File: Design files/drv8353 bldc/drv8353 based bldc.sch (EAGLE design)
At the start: 115 parts, among them IC1 DRV8353RSRGZT, J3 2X6 FEMALE, J4 B06B-HCMKK

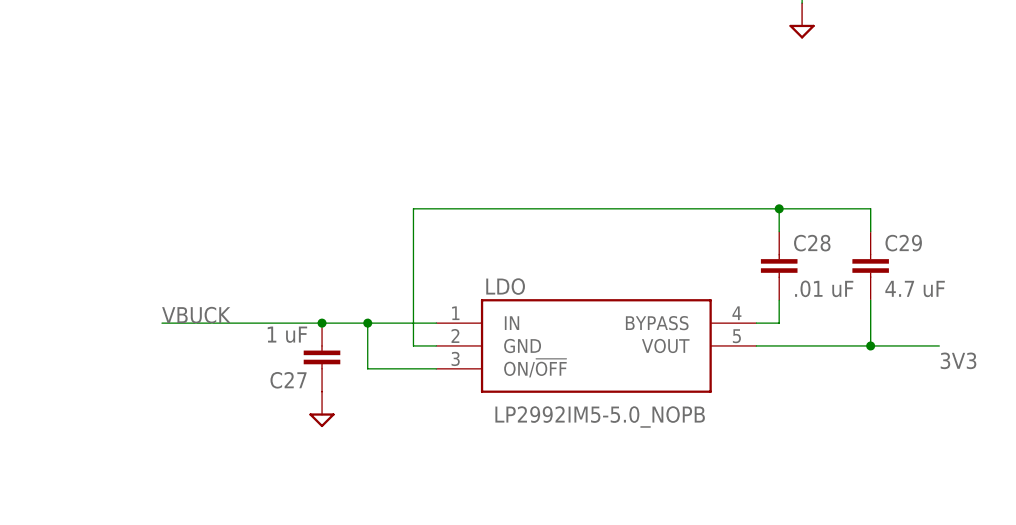
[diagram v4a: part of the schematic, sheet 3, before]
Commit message: adds zener and bypas header for LDO
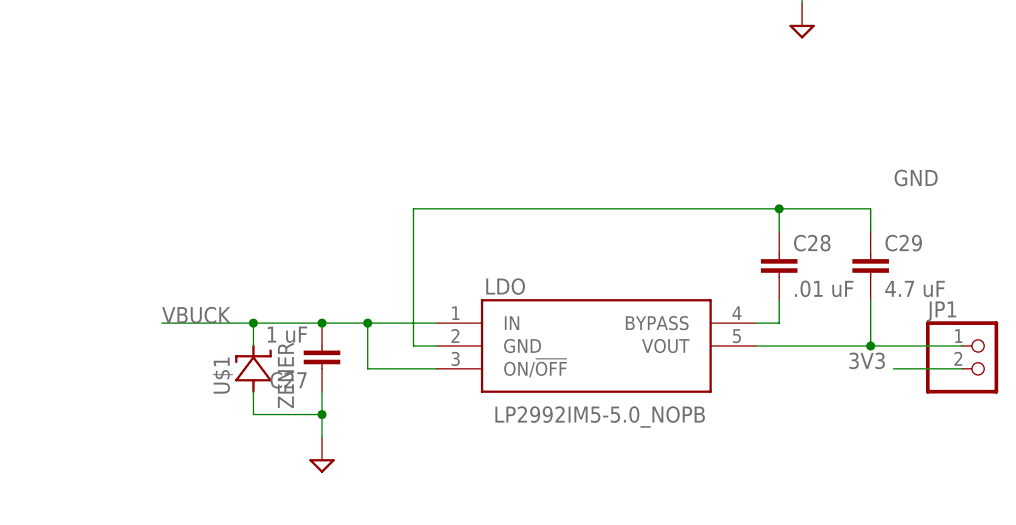
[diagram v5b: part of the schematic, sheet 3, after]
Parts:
- added JP1: (no value), pinhead:PINHD-1X2
- added U$1: ZENER, REV BLDC:ZENER
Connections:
- removed net N$5: C28.1, C29.1, LDO.GND
- new net N$2: C29.2, JP1.1, LDO.VOUT
- net 3V3: now also JP1.2; no longer C29.2, LDO.VOUT
- net GND: now also C28.1, C29.1, LDO.GND, U$1.A
- net VBUCK: now also U$1.C
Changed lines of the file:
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@@
 <part name="D6" library="REV BLDC" deviceset="D-" device="SOD123" package3d_urn="urn:adsk.eagle:package:26308/2"/>
 <part name="D7" library="REV BLDC" deviceset="D-" device="SOD123" package3d_urn="urn:adsk.eagle:package:26308/2"/>
+<part name="U$1" library="REV BLDC" deviceset="ZENER" device="" package3d_urn="urn:adsk.eagle:package:26308/2"/>
+<part name="JP1" library="pinhead" library_urn="urn:adsk.eagle:library:325" deviceset="PINHD-1X2" device="" package3d_urn="urn:adsk.eagle:package:22435/2"/>
 </parts>
 <sheets>
@@
 <attribute name="VALUE" x="197.104" y="0.381" size="1.778" layer="96"/>
 </instance>
-<instance part="SUPPLY7" gate="GND" x="134.62" y="-12.7" smashed="yes"/>
+<instance part="SUPPLY7" gate="GND" x="134.62" y="-17.78" smashed="yes"/>
 <instance part="J4" gate="G$1" x="25.4" y="-15.24" smashed="yes">
 <attribute name="NAME" x="41.91" y="-7.62" size="1.778" layer="95" align="center-left"/>
@@
 <instance part="U$7" gate="G$1" x="55.88" y="10.16" smashed="yes"/>
 <instance part="U$8" gate="G$1" x="55.88" y="7.62" smashed="yes"/>
+<instance part="U$1" gate="G$1" x="127" y="-7.62" smashed="yes" rot="R90">
+<attribute name="NAME" x="124.3584" y="-10.5664" size="1.778" layer="95" rot="R90"/>
+<attribute name="VALUE" x="131.4958" y="-12.0904" size="1.778" layer="96" rot="R90"/>
+</instance>
+<instance part="JP1" gate="G$1" x="208.28" y="-7.62" smashed="yes">
+<attribute name="NAME" x="201.93" y="-1.905" size="1.778" layer="95"/>
+<attribute name="VALUE" x="201.93" y="-12.7" size="1.778" layer="96"/>
+</instance>
 </instances>
 <busses>
@@
 <pinref part="C27" gate="G$1" pin="1"/>
 <pinref part="SUPPLY7" gate="GND" pin="GND"/>
+<wire x1="134.62" y1="-15.24" x2="134.62" y2="-12.7" width="0.1524" layer="91"/>
+<pinref part="U$1" gate="G$1" pin="A"/>
+<wire x1="134.62" y1="-12.7" x2="134.62" y2="-10.16" width="0.1524" layer="91"/>
+<wire x1="127" y1="-10.16" x2="127" y2="-12.7" width="0.1524" layer="91"/>
+<wire x1="127" y1="-12.7" x2="134.62" y2="-12.7" width="0.1524" layer="91"/>
+<junction x="134.62" y="-12.7"/>
 </segment>
 <segment>
@@
 <wire x1="45.72" y1="-20.32" x2="55.88" y2="-20.32" width="0.1524" layer="91"/>
 <label x="55.88" y="-20.32" size="1.778" layer="95"/>
+</segment>
+<segment>
+<pinref part="LDO" gate="G$1" pin="GND"/>
+<wire x1="147.32" y1="-5.08" x2="144.78" y2="-5.08" width="0.1524" layer="91"/>
+<wire x1="144.78" y1="-5.08" x2="144.78" y2="10.16" width="0.1524" layer="91"/>
+<wire x1="144.78" y1="10.16" x2="185.42" y2="10.16" width="0.1524" layer="91"/>
+<pinref part="C28" gate="G$1" pin="1"/>
+<wire x1="185.42" y1="10.16" x2="195.58" y2="10.16" width="0.1524" layer="91"/>
+<wire x1="185.42" y1="7.62" x2="185.42" y2="10.16" width="0.1524" layer="91"/>
+<junction x="185.42" y="10.16"/>
+<pinref part="C29" gate="G$1" pin="1"/>
+<wire x1="195.58" y1="7.62" x2="195.58" y2="10.16" width="0.1524" layer="91"/>
+<label x="198.12" y="12.7" size="1.778" layer="95"/>
 </segment>
 </net>
@@
 <pinref part="LDO" gate="G$1" pin="ON/!OFF"/>
 <wire x1="139.7" y1="-2.54" x2="134.62" y2="-2.54" width="0.1524" layer="91"/>
-<wire x1="134.62" y1="-2.54" x2="116.84" y2="-2.54" width="0.1524" layer="91"/>
+<wire x1="134.62" y1="-2.54" x2="127" y2="-2.54" width="0.1524" layer="91"/>
+<wire x1="127" y1="-2.54" x2="116.84" y2="-2.54" width="0.1524" layer="91"/>
 <wire x1="147.32" y1="-7.62" x2="139.7" y2="-7.62" width="0.1524" layer="91"/>
 <wire x1="139.7" y1="-7.62" x2="139.7" y2="-2.54" width="0.1524" layer="91"/>
@@
 <pinref part="C27" gate="G$1" pin="2"/>
 <junction x="134.62" y="-2.54"/>
+<pinref part="U$1" gate="G$1" pin="C"/>
+<wire x1="127" y1="-5.08" x2="127" y2="-2.54" width="0.1524" layer="91"/>
+<junction x="127" y="-2.54"/>
 </segment>
 </net>
 <net name="3V3" class="0">
-<segment>
-<pinref part="LDO" gate="G$1" pin="VOUT"/>
-<wire x1="182.88" y1="-5.08" x2="195.58" y2="-5.08" width="0.1524" layer="91"/>
-<pinref part="C29" gate="G$1" pin="2"/>
-<wire x1="195.58" y1="-5.08" x2="203.2" y2="-5.08" width="0.1524" layer="91"/>
-<wire x1="195.58" y1="0" x2="195.58" y2="-5.08" width="0.1524" layer="91"/>
-<junction x="195.58" y="-5.08"/>
-<label x="203.2" y="-7.62" size="1.778" layer="95"/>
-</segment>
 <segment>
 <pinref part="J4" gate="G$1" pin="2"/>
@@
 <label x="55.88" y="-15.24" size="1.778" layer="95"/>
 </segment>
-</net>
-<net name="N$5" class="0">
-<segment>
-<pinref part="LDO" gate="G$1" pin="GND"/>
-<wire x1="147.32" y1="-5.08" x2="144.78" y2="-5.08" width="0.1524" layer="91"/>
-<wire x1="144.78" y1="-5.08" x2="144.78" y2="10.16" width="0.1524" layer="91"/>
-<wire x1="144.78" y1="10.16" x2="185.42" y2="10.16" width="0.1524" layer="91"/>
-<pinref part="C28" gate="G$1" pin="1"/>
-<wire x1="185.42" y1="10.16" x2="195.58" y2="10.16" width="0.1524" layer="91"/>
-<wire x1="185.42" y1="7.62" x2="185.42" y2="10.16" width="0.1524" layer="91"/>
-<junction x="185.42" y="10.16"/>
-<pinref part="C29" gate="G$1" pin="1"/>
-<wire x1="195.58" y1="7.62" x2="195.58" y2="10.16" width="0.1524" layer="91"/>
+<segment>
+<pinref part="JP1" gate="G$1" pin="2"/>
+<wire x1="205.74" y1="-7.62" x2="198.12" y2="-7.62" width="0.1524" layer="91"/>
+<label x="193.04" y="-7.62" size="1.778" layer="95"/>
 </segment>
 </net>
@@
 </segment>
 </net>
+<net name="N$2" class="0">
+<segment>
+<pinref part="LDO" gate="G$1" pin="VOUT"/>
+<wire x1="182.88" y1="-5.08" x2="195.58" y2="-5.08" width="0.1524" layer="91"/>
+<pinref part="C29" gate="G$1" pin="2"/>
+<wire x1="195.58" y1="-5.08" x2="195.58" y2="0" width="0.1524" layer="91"/>
+<junction x="195.58" y="-5.08"/>
+<pinref part="JP1" gate="G$1" pin="1"/>
+<wire x1="195.58" y1="-5.08" x2="205.74" y2="-5.08" width="0.1524" layer="91"/>
+</segment>
+</net>

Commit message: silkscreen pass, slightly moved fuse to prevent part collision
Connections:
- net VBUCK: now also U$1.LINE; no longer U$1.C
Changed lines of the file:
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@@
 <pinref part="C27" gate="G$1" pin="2"/>
 <junction x="134.62" y="-2.54"/>
-<pinref part="U$1" gate="G$1" pin="C"/>
+<pinref part="U$1" gate="G$1" pin="LINE"/>
 <wire x1="127" y1="-5.08" x2="127" y2="-2.54" width="0.1524" layer="91"/>
 <junction x="127" y="-2.54"/>

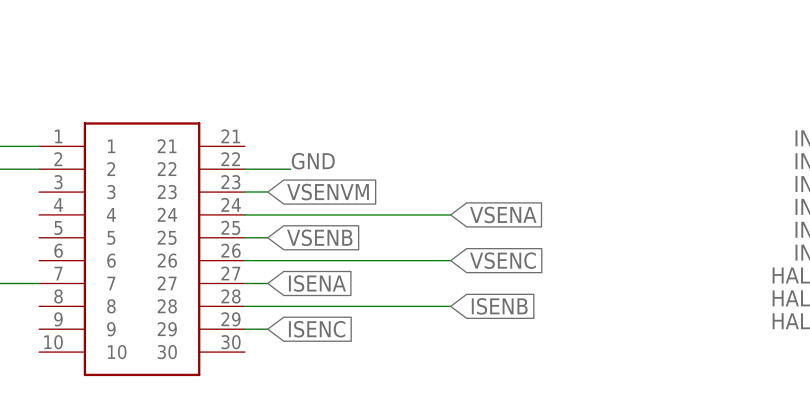
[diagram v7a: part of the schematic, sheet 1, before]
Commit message: moves VSENA away from ADC B; got rid of some vias by the text
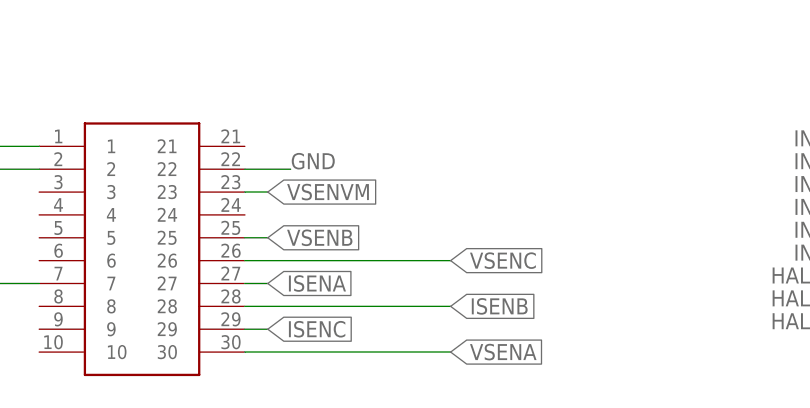
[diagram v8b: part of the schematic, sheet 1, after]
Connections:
- net VSENA: now also U$2.30; no longer U$2.24
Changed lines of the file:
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@@
 <?xml version="1.0" encoding="utf-8"?>
 <!DOCTYPE eagle SYSTEM "eagle.dtd">
-<eagle version="9.5.0">
+<eagle version="9.5.1">
 <drawing>
 <settings>
@@
 </segment>
 </net>
-<net name="VSENA" class="0">
-<segment>
-<wire x1="-45.72" y1="-124.46" x2="-22.86" y2="-124.46" width="0.1524" layer="91"/>
-<label x="-22.86" y="-124.46" size="1.778" layer="95" xref="yes"/>
-<pinref part="U$2" gate="G$1" pin="24"/>
-</segment>
-</net>
 <net name="GHB" class="0">
 <segment>
@@
 </segment>
 </net>
+<net name="VSENA" class="0">
+<segment>
+<pinref part="U$2" gate="G$1" pin="30"/>
+<wire x1="-45.72" y1="-139.7" x2="-22.86" y2="-139.7" width="0.1524" layer="91"/>
+<label x="-22.86" y="-139.7" size="1.778" layer="95" xref="yes"/>
+</segment>
+</net>
